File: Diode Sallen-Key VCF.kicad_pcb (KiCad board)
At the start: 2 copper layers, 75 x 105 mm, 89 parts, among them J10 Conn_02x05_Odd_Even, J11 Conn_01x01, J12 Conn_01x01, J13 Conn_01x01, J14 Conn_01x01, J15 Conn_01x01, J16 Conn_01x01, J17 Conn_01x01, J18 Conn_01x01, J19 Conn_01x01, J20 Conn_01x01, J4 Conn_01x01, J5 Conn_01x01, J6 Conn_01x01, J7 Conn_01x01, J8 Conn_01x01, J9 Conn_01x01, U1 TL072, U2 TL072, U3 TL072, U4 TL072, U5 TL072, U6 TL072, U7 TL072

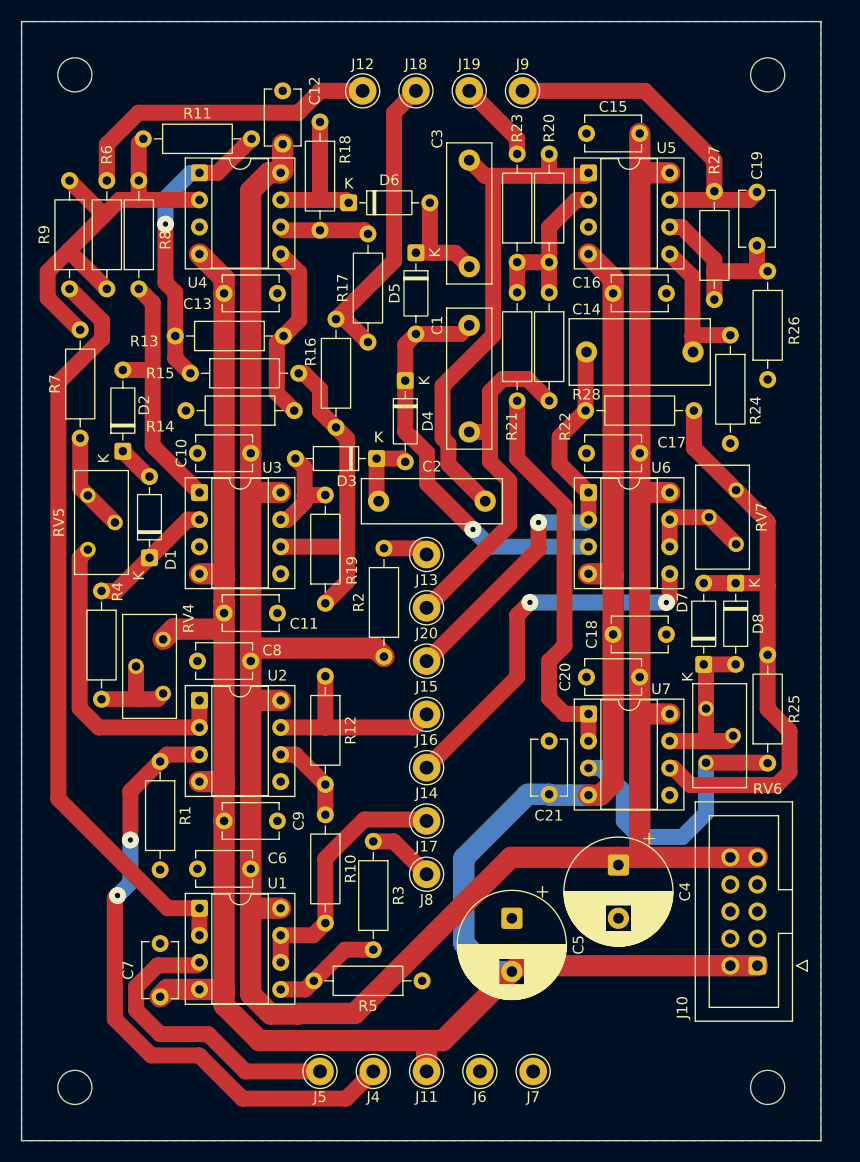
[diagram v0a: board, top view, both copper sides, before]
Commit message: Quad opamps
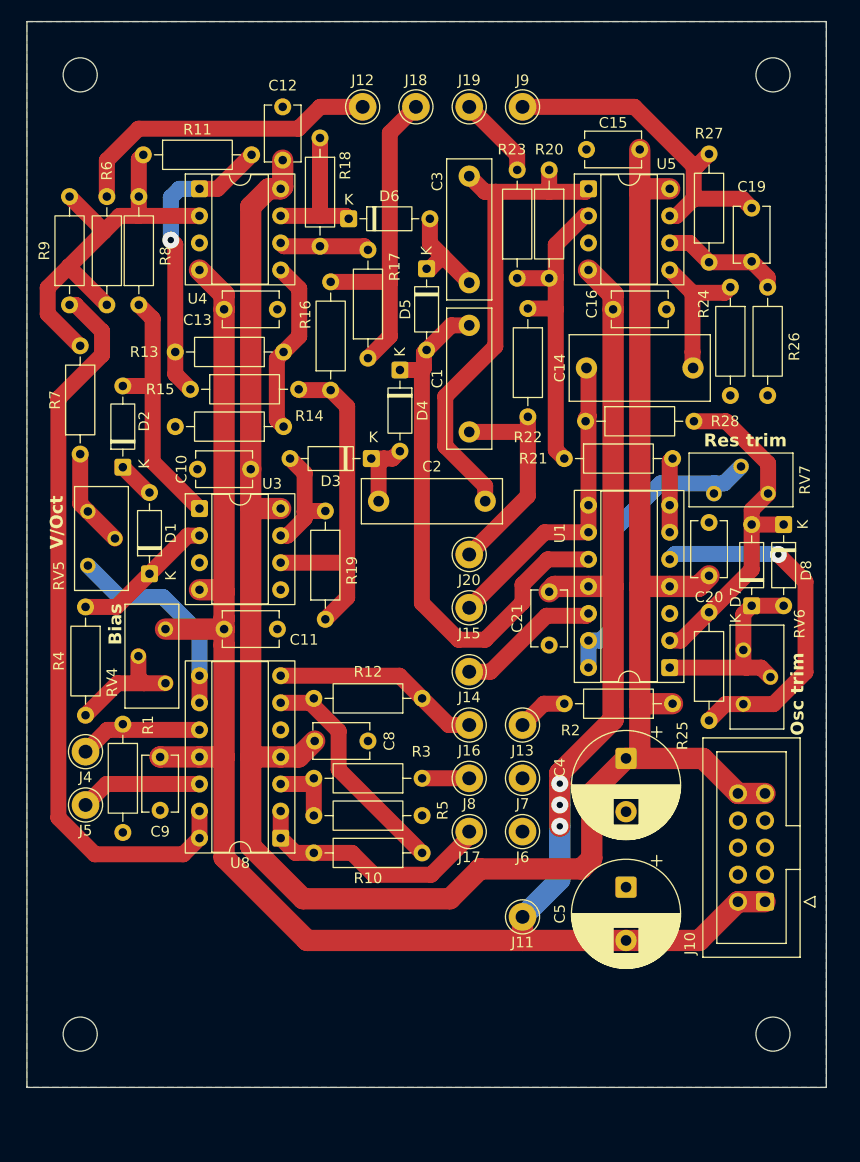
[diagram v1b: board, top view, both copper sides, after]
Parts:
- removed C17, C18, C6, C7: 0.1u, Capacitor_THT:C_Disc_D5.1mm_W3.2mm_P5.00mm
- removed U2, U6, U7: TL072, Package_DIP:DIP-8_W7.62mm_Socket
- added U8: TL074, Package_DIP:DIP-14_W7.62mm_Socket, F.Cu at (138.8, 116.1)
- U1: value TL072 -> TL074; footprint Package_DIP:DIP-8_W7.62mm_Socket -> Package_DIP:DIP-14_W7.62mm_Socket
- moved U1 49.6 mm to (175.3, 100.1), turned to 180 degrees
- moved J4 40.4 mm to (120.5, 108.0)
- moved J5 33.3 mm to (120.5, 113.0)
- moved J7 27.5 mm to (161.5, 110.5)
- moved R2 27.4 mm to (175.6, 103.5), turned to 180 degrees
- moved J6 22.9 mm to (161.5, 115.5)
- moved J13 18.4 mm to (161.5, 105.5)
- moved J11 17.1 mm to (161.5, 123.5)
- moved R21 16.2 mm to (165.4, 80.5), turned to 0 degrees
- moved R5 15.5 mm to (152.1, 114.0)
- moved C20 11.5 mm to (179.0, 91.5), turned to 90 degrees
- moved C5 11.1 mm to (171.2, 120.7)
- moved C9 11.0 mm to (127.5, 113.5), turned to 90 degrees
- moved C4 10.0 mm to (171.2, 108.6)
- moved J14 9.85 mm to (156.5, 100.5)
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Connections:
- R21 pad 2: Net-(U7A--) -> Net-(U1B--)
- R25 pad 1: Net-(U7A-+) -> Net-(U1B-+)
- R3 pad 2: Net-(U1B-+) -> Net-(U8A-+)
- R5 pad 2: Net-(U1B-+) -> Net-(U8A-+)
- R9 pad 1: Net-(U1A--) -> Net-(U8D--)
- RV6 pad 3: Net-(U7A-+) -> Net-(U1B-+)
- RV7 pad 1: Net-(U6B--) -> Net-(U1D--)
- RV7 pad 2: Net-(U6B--) -> Net-(U1D--)
- U1 pad 1: Net-(U1A--) -> Net-(D7-K)
- U1 pad 2: Net-(U1A--) -> Net-(D7-A)
- U1 pad 3: /CV_IN -> GND
- U1 pad 4: VEE -> VCC
- U1 pad 6: /IN_BUF -> Net-(U1B--)
- U1 pad 7: /IN_BUF -> Net-(U1B--)
- U1 pad 8: VCC -> /OUT_BUF
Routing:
- net Net-(U1A--): track 70.9 -> 0.00 mm
- net Net-(U8D--): track 0.00 -> 69.2 mm
- net /VOCT_IN: track 58.3 -> 12.1 mm, vias 2 -> 0
- net Net-(U7A--): track 37.2 -> 0.00 mm
- net Net-(U1D--): track 0.00 -> 29.9 mm
- net VCC: track 235.0 -> 206.6 mm
- net Net-(U7A-+): track 26.8 -> 0.00 mm
- net VEE: track 229.4 -> 203.0 mm, vias 0 -> 3
- net Net-(D7-A): track 56.2 -> 32.6 mm
- net Net-(U1B-+): track 10.2 -> 33.4 mm, vias 0 -> 1
- net /RES_WIPER: track 35.1 -> 13.5 mm, vias 2 -> 0
- net /CV_IN: track 28.7 -> 11.5 mm
- net /FB_INV_SUM: track 16.7 -> 30.9 mm
- net Net-(D4-K): track 38.3 -> 52.1 mm, vias 1 -> 0
- net Net-(U8B--): track 8.19 -> 21.8 mm
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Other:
- board size 75 x 105 mm -> 75 x 100 mm
- board text added: "Bias"
- board text added: "Osc trim"
- board text added: "Res trim"
- board text added: "V/Oct"

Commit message: small tweaks
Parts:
- R1: value 100k -> 1M
- moved R28 1.42 mm to (166.0, 77.0)
- moved RV7 1.39 mm to (180.0, 82.5)
- moved D7 1.12 mm to (183.5, 93.3)
- moved D8 1.12 mm to (186.5, 85.7)
- moved R22 1.00 mm to (161.0, 66.4)
- renumbered C12 to C10, C13 to C11, C14 to C12, C15 to C13, C16 to C14, C20 to C15, C21 to C16, C19 to C17, C8 to C6, C9 to C7, C10 to C8, C11 to C9, R26 to R25, R25 to R26, U8 to U1, U3 to U2, U4 to U3, U5 to U4, U1 to U5
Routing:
- net Net-(U5B-+): track 33.4 -> 26.1 mm, vias 1 -> 0
- net Net-(D7-A): track 32.6 -> 34.9 mm
- net /HP_IN: track 20.7 -> 19.3 mm
- net /OUT_BUF: track 30.2 -> 31.5 mm
- net Net-(D7-K): track 19.1 -> 20.3 mm
- net /FB_INV_SUM: track 30.9 -> 31.4 mm

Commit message: small tweaks
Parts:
- added R2: 12k, Resistor_THT:R_Axial_DIN0207_L6.3mm_D2.5mm_P10.16mm_Horizontal, F.Cu at (141.9, 114.0)
- moved R11 3.50 mm to (152.1, 121.0)
- moved R6 3.50 mm to (152.1, 117.5)
- renumbered R8 to R10, R10 to R11, R11 to R12, R12 to R13, R13 to R14, R14 to R15, R15 to R16, R16 to R17, R17 to R18, R18 to R19, R19 to R20, R20 to R21, R21 to R22, R22 to R23, R23 to R24, R24 to R25, R25 to R26, R26 to R27, R27 to R28, R28 to R29, R2 to R3, R3 to R4, R4 to R5, R5 to R6, R9 to R7, R6 to R8, R7 to R9
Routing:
- net /IN_BUF: track 23.1 -> 29.6 mm
- net Net-(U1A-+): track 6.83 -> 11.8 mm
- net VCC: track 206.6 -> 210.3 mm
- net Net-(U1B--): track 21.8 -> 25.3 mm
- net /AUDIO_IN: track 4.42 -> 7.92 mm
- net VEE: track 203.0 -> 205.6 mm

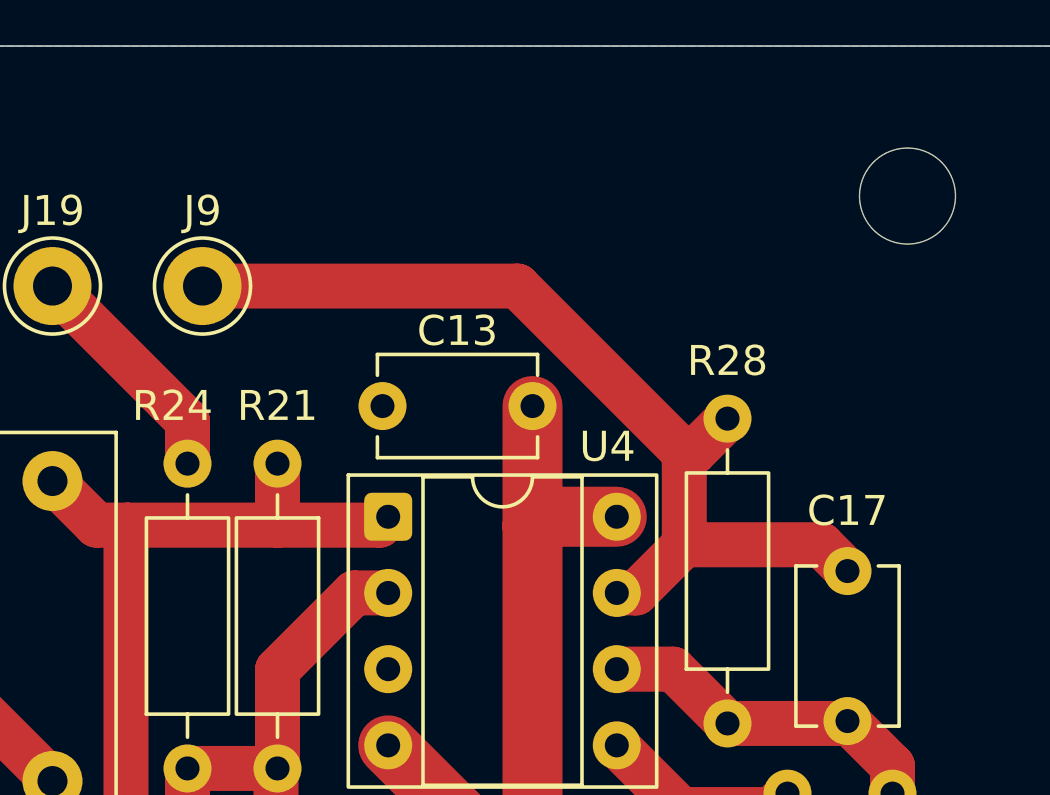
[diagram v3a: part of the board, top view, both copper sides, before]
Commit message: missed output resistor
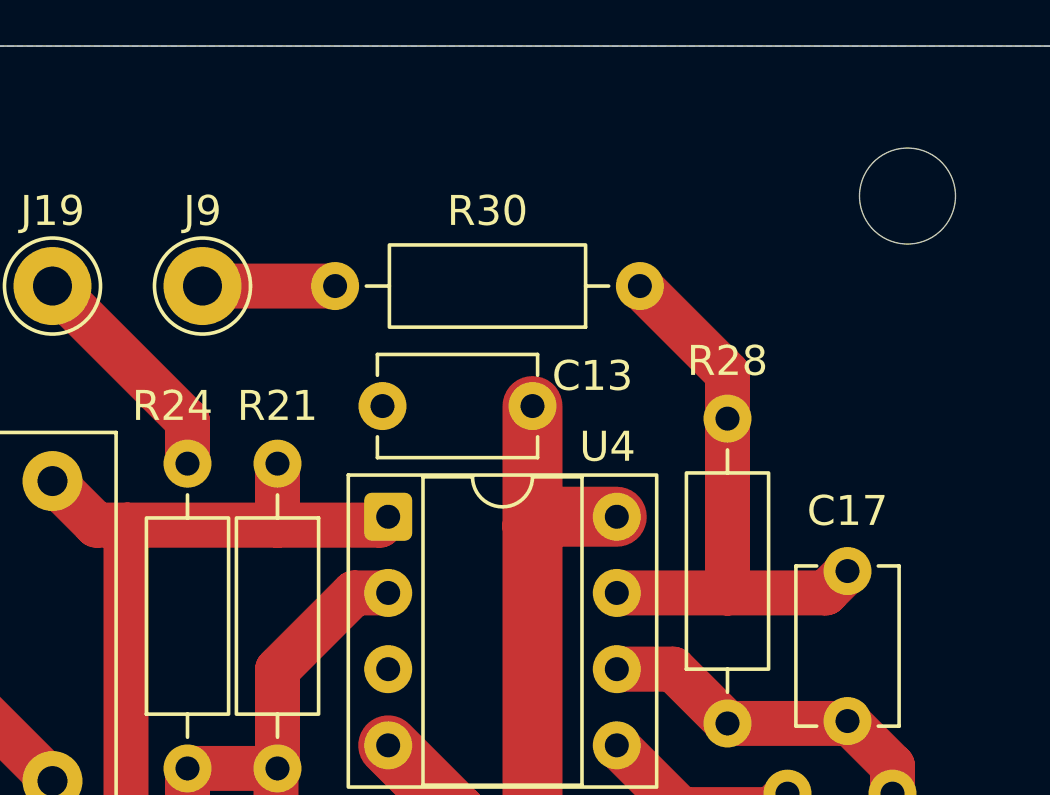
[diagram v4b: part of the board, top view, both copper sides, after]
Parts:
- added R30: 1k, Resistor_THT:R_Axial_DIN0207_L6.3mm_D2.5mm_P10.16mm_Horizontal, F.Cu at (176.1, 47.5)
- C17: value 10p -> 22p
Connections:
- C17 pad 2: /AUDIO_OUT -> Net-(C17-Pad2)
- R28 pad 2: /AUDIO_OUT -> Net-(C17-Pad2)
- U4 pad 7: /AUDIO_OUT -> Net-(C17-Pad2)
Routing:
- net /AUDIO_OUT: track 32.1 -> 4.42 mm
- net Net-(C17-Pad2): track 0.00 -> 19.4 mm
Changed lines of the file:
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@@
 		(filling no)
 		(pcbplotparams
-			(layerselection 0x00000000_00000000_55555555_5755f5ff)
+			(layerselection 0x00000000_00000000_55555555_5755557f)
 			(plot_on_all_layers_selection 0x00000000_00000000_00000000_00000000)
 			(disableapertmacros no)
 			(usegerberextensions no)
 			(usegerberattributes yes)
-			(usegerberadvancedattributes yes)
-			(creategerberjobfile yes)
+			(usegerberadvancedattributes no)
+			(creategerberjobfile no)
 			(dashed_line_dash_ratio 12)
 			(dashed_line_gap_ratio 3)
@@
 			(sketchdnponfab yes)
 			(crossoutdnponfab yes)
-			(subtractmaskfromsilk no)
+			(subtractmaskfromsilk yes)
 			(outputformat 1)
 			(mirror no)
-			(drillshape 1)
+			(drillshape 0)
 			(scaleselection 1)
-			(outputdirectory "")
+			(outputdirectory "./CAM")
 		)
 	)
@@
 			)
 		)
-		(property "Value" "10p"
+		(property "Value" "22p"
 			(at 2.5 2.85 90)
 			(layer "F.Fab")
@@
 			(layers "*.Cu" "*.Mask")
 			(remove_unused_layers no)
-			(net "/AUDIO_OUT")
+			(net "Net-(C17-Pad2)")
 			(pintype "passive")
 		)
@@
 			(layers "*.Cu" "*.Mask")
 			(remove_unused_layers no)
-			(net "/AUDIO_OUT")
+			(net "Net-(C17-Pad2)")
 			(pintype "output")
 		)
@@
 		(tags "C Disc series Radial pin pitch 5.00mm diameter 5.1mm width 3.2mm Capacitor")
 		(property "Reference" "C13"
-			(at 2.5 2.5 180)
+			(at -2 1 180)
 			(layer "F.SilkS")
 			(effects
@@
 		)
 		(property "Value" "0.1u"
-			(at 2.5 2.85 180)
+			(at -2 0 180)
 			(layer "F.Fab")
 			(effects
@@
 			(layers "*.Cu" "*.Mask")
 			(remove_unused_layers no)
-			(net "/AUDIO_OUT")
+			(net "Net-(C17-Pad2)")
 			(pintype "passive")
 		)
@@
 		)
 	)
+	(footprint "Resistor_THT:R_Axial_DIN0207_L6.3mm_D2.5mm_P10.16mm_Horizontal"
+		(layer "F.Cu")
+		(at 176.08 47.5 180)
+		(descr "Resistor, Axial_DIN0207 series, Axial, Horizontal, pin pitch=10.16mm, 0.25W = 1/4W, length*diameter=6.3*2.5mm^2, http://cdn-reichelt.de/documents/datenblatt/B400/1_4W%23YAG.pdf")
+		(tags "Resistor Axial_DIN0207 series Axial Horizontal pin pitch 10.16mm 0.25W = 1/4W length 6.3mm diameter 2.5mm")
+		(property "Reference" "R30"
+			(at 5.08 2.5 0)
+			(layer "F.SilkS")
+			(effects
+				(font
+					(size 1 1)
+					(thickness 0.15)
+				)
+			)
+		)
+		(property "Value" "1k"
+			(at 5.08 2.37 0)
+			(layer "F.Fab")
+			(effects
+				(font
+					(size 1 1)
+					(thickness 0.15)
+				)
+			)
+		)
+		(property "Datasheet" ""
+			(at 0 0 0)
+			(layer "F.Fab")
+			(hide yes)
+			(effects
+				(font
+					(size 1.27 1.27)
+				)
+			)
+		)
+		(property "Description" "Resistor"
+			(at 0 0 0)
+			(layer "F.Fab")
+			(hide yes)
+			(effects
+				(font
+					(size 1.27 1.27)
+				)
+			)
+		)
+		(property ki_fp_filters "R_*")
+		(sheetname "/")
+		(sheetfile "Diode Sallen-Key VCF.kicad_sch")
+		(units
+			(unit
+				(name "A")
+				(pins "1" "2")
+			)
+		)
+		(attr through_hole)
+		(duplicate_pad_numbers_are_jumpers no)
+		(fp_line
+			(start 9.12 0)
+			(end 8.35 0)
+			(stroke
+				(width 0.12)
+				(type solid)
+			)
+			(layer "F.SilkS")
+		)
+		(fp_line
+			(start 1.04 0)
+			(end 1.81 0)
+			(stroke
+				(width 0.12)
+				(type solid)
+			)
+			(layer "F.SilkS")
+		)
+		(fp_rect
+			(start 1.81 -1.37)
+			(end 8.35 1.37)
+			(stroke
+				(width 0.12)
+				(type solid)
+			)
+			(fill no)
+			(layer "F.SilkS")
+		)
+		(fp_rect
+			(start -1.05 -1.5)
+			(end 11.21 1.5)
+			(stroke
+				(width 0.05)
+				(type solid)
+			)
+			(fill no)
+			(layer "F.CrtYd")
+		)
+		(fp_line
+			(start 10.16 0)
+			(end 8.23 0)
+			(stroke
+				(width 0.1)
+				(type solid)
+			)
+			(layer "F.Fab")
+		)
+		(fp_line
+			(start 0 0)
+			(end 1.93 0)
+			(stroke
+				(width 0.1)
+				(type solid)
+			)
+			(layer "F.Fab")
+		)
+		(fp_rect
+			(start 1.93 -1.25)
+			(end 8.23 1.25)
+			(stroke
+				(width 0.1)
+				(type solid)
+			)
+			(fill no)
+			(layer "F.Fab")
+		)
+		(fp_text user "${REFERENCE}"
+			(at 5.08 0 0)
+			(layer "F.Fab")
+			(effects
+				(font
+					(size 1 1)
+					(thickness 0.15)
+				)
+			)
+		)
+		(pad "1" thru_hole circle
+			(at 0 0 180)
+			(size 1.6 1.6)
+			(drill 0.8)
+			(layers "*.Cu" "*.Mask")
+			(remove_unused_layers no)
+			(net "Net-(C17-Pad2)")
+			(pintype "passive")
+		)
+		(pad "2" thru_hole circle
+			(at 10.16 0 180)
+			(size 1.6 1.6)
+			(drill 0.8)
+			(layers "*.Cu" "*.Mask")
+			(remove_unused_layers no)
+			(net "/AUDIO_OUT")
+			(pintype "passive")
+		)
+		(embedded_fonts no)
+		(model "${KICAD10_3DMODEL_DIR}/Resistor_THT.3dshapes/R_Axial_DIN0207_L6.3mm_D2.5mm_P10.16mm_Horizontal.step"
+			(offset
+				(xyz 0 0 0)
+			)
+			(scale
+				(xyz 1 1 1)
+			)
+			(rotate
+				(xyz 0 0 0)
+			)
+		)
+	)
 	(footprint "Potentiometer_THT:Potentiometer_Bourns_3296Y_Vertical"
 		(layer "F.Cu")
@@
 		)
 		(property "Value" "TL074"
-			(at 3.81 17.57 0)
+			(at 3.81 5.615 0)
 			(layer "F.Fab")
 			(effects
@@
 		)
 		(fp_text user "${REFERENCE}"
-			(at 3.81 7.62 90)
+			(at 3.81 7.62 180)
 			(layer "F.Fab")
 			(effects
@@
 	)
 	(segment
-		(start 175.951981 57.73)
-		(end 177.56 56.121981)
-		(width 1.5)
-		(layer "F.Cu")
-		(net "/AUDIO_OUT")
-	)
-	(segment
-		(start 172 47.5)
+		(start 165.92 47.5)
 		(end 161.5 47.5)
 		(width 1.5)
@@
 	)
 	(segment
-		(start 177.56 56.121981)
-		(end 177.56 53.06)
-		(width 1.5)
-		(layer "F.Cu")
-		(net "/AUDIO_OUT")
-	)
-	(segment
-		(start 177.86 53.06)
-		(end 177.56 53.06)
-		(width 1.5)
-		(layer "F.Cu")
-		(net "/AUDIO_OUT")
-	)
-	(segment
-		(start 177.56 53.06)
-		(end 172 47.5)
-		(width 1.5)
-		(layer "F.Cu")
-		(net "/AUDIO_OUT")
-	)
-	(segment
-		(start 175.31 57.73)
-		(end 175.951981 57.73)
-		(width 1.5)
-		(layer "F.Cu")
-		(net "/AUDIO_OUT")
-	)
-	(segment
-		(start 183 57)
-		(end 182.121981 56.121981)
-		(width 1.5)
-		(layer "F.Cu")
-		(net "/AUDIO_OUT")
-	)
-	(segment
-		(start 182.121981 56.121981)
-		(end 177.56 56.121981)
-		(width 1.5)
-		(layer "F.Cu")
-		(net "/AUDIO_OUT")
-	)
-	(segment
-		(start 179 51.92)
-		(end 177.86 53.06)
-		(width 1.5)
-		(layer "F.Cu")
-		(net "/AUDIO_OUT")
-	)
-	(segment
 		(start 126.8 74)
 		(end 126.8 80.8)
@@
 	)
 	(segment
+		(start 120.72 85.46)
+		(end 120 84.74)
+		(width 1.5)
+		(layer "F.Cu")
+		(net "Net-(R9-Pad1)")
+	)
+	(segment
+		(start 123.26 88)
+		(end 120.72 85.46)
+		(width 1.5)
+		(layer "F.Cu")
+		(net "Net-(R9-Pad1)")
+	)
+	(segment
+		(start 120 84.74)
+		(end 120 80.08)
+		(width 1.5)
+		(layer "F.Cu")
+		(net "Net-(R9-Pad1)")
+	)
+	(segment
 		(start 131.19 116.115)
 		(end 129.675 117.63)
@@
 	)
 	(segment
+		(start 123.5 101.58)
+		(end 126 101.58)
+		(width 1.5)
+		(layer "F.Cu")
+		(net "Net-(R5-Pad2)")
+	)
+	(segment
+		(start 126 101.58)
+		(end 128 101.58)
+		(width 1.5)
+		(layer "F.Cu")
+		(net "Net-(R5-Pad2)")
+	)
+	(segment
+		(start 125.46 101.04)
+		(end 126 101.58)
+		(width 1.5)
+		(layer "F.Cu")
+		(net "Net-(R5-Pad2)")
+	)
+	(segment
+		(start 125.46 99.04)
+		(end 125.46 101.04)
+		(width 1.5)
+		(layer "F.Cu")
+		(net "Net-(R5-Pad2)")
+	)
+	(segment
+		(start 120.5 104.58)
+		(end 123.5 101.58)
+		(width 1.5)
+		(layer "F.Cu")
+		(net "Net-(R5-Pad2)")
+	)
+	(segment
 		(start 182.5 100.115)
 		(end 183.875 100.115)
@@
 	)
 	(segment
-		(start 123.5 101.58)
-		(end 126 101.58)
+		(start 179 57.73)
+		(end 175.31 57.73)
 		(width 1.5)
 		(layer "F.Cu")
-		(net "Net-(R5-Pad2)")
-	)
-	(segment
-		(start 126 101.58)
-		(end 128 101.58)
-		(width 1.5)
-		(layer "F.Cu")
-		(net "Net-(R5-Pad2)")
-	)
-	(segment
-		(start 125.46 101.04)
-		(end 126 101.58)
-		(width 1.5)
-		(layer "F.Cu")
-		(net "Net-(R5-Pad2)")
+		(net "Net-(C17-Pad2)")
 	)
 	(segment
-		(start 125.46 99.04)
-		(end 125.46 101.04)
+		(start 179 51.92)
+		(end 179 57.73)
 		(width 1.5)
 		(layer "F.Cu")
-		(net "Net-(R5-Pad2)")
+		(net "Net-(C17-Pad2)")
 	)
 	(segment
-		(start 120.5 104.58)
-		(end 123.5 101.58)
+		(start 179 50.42)
+		(end 176.08 47.5)
 		(width 1.5)
 		(layer "F.Cu")
-		(net "Net-(R5-Pad2)")
+		(net "Net-(C17-Pad2)")
 	)
 	(segment
-		(start 120.72 85.46)
-		(end 120 84.74)
+		(start 179 51.92)
+		(end 179 50.42)
 		(width 1.5)
 		(layer "F.Cu")
-		(net "Net-(R9-Pad1)")
+		(net "Net-(C17-Pad2)")
 	)
 	(segment
-		(start 123.26 88)
-		(end 120.72 85.46)
+		(start 183 57)
+		(end 182.27 57.73)
 		(width 1.5)
 		(layer "F.Cu")
-		(net "Net-(R9-Pad1)")
+		(net "Net-(C17-Pad2)")
 	)
 	(segment
-		(start 120 84.74)
-		(end 120 80.08)
+		(start 182.27 57.73)
+		(end 179 57.73)
 		(width 1.5)
 		(layer "F.Cu")
-		(net "Net-(R9-Pad1)")
+		(net "Net-(C17-Pad2)")
 	)
 	(zone
